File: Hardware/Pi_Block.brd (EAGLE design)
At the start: 30.5 x 94 mm, 54 parts, among them Q1 200mA/50V, U1 PCA9306, U2 EDISON_CONNECTOR_FULLMOUNTING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, U3 EDISON_CONNECTOR_FULLHEADER, U4 TPS62065, U5 MIC5219 3.3V, U6 TXB0108, U7 TXB0108

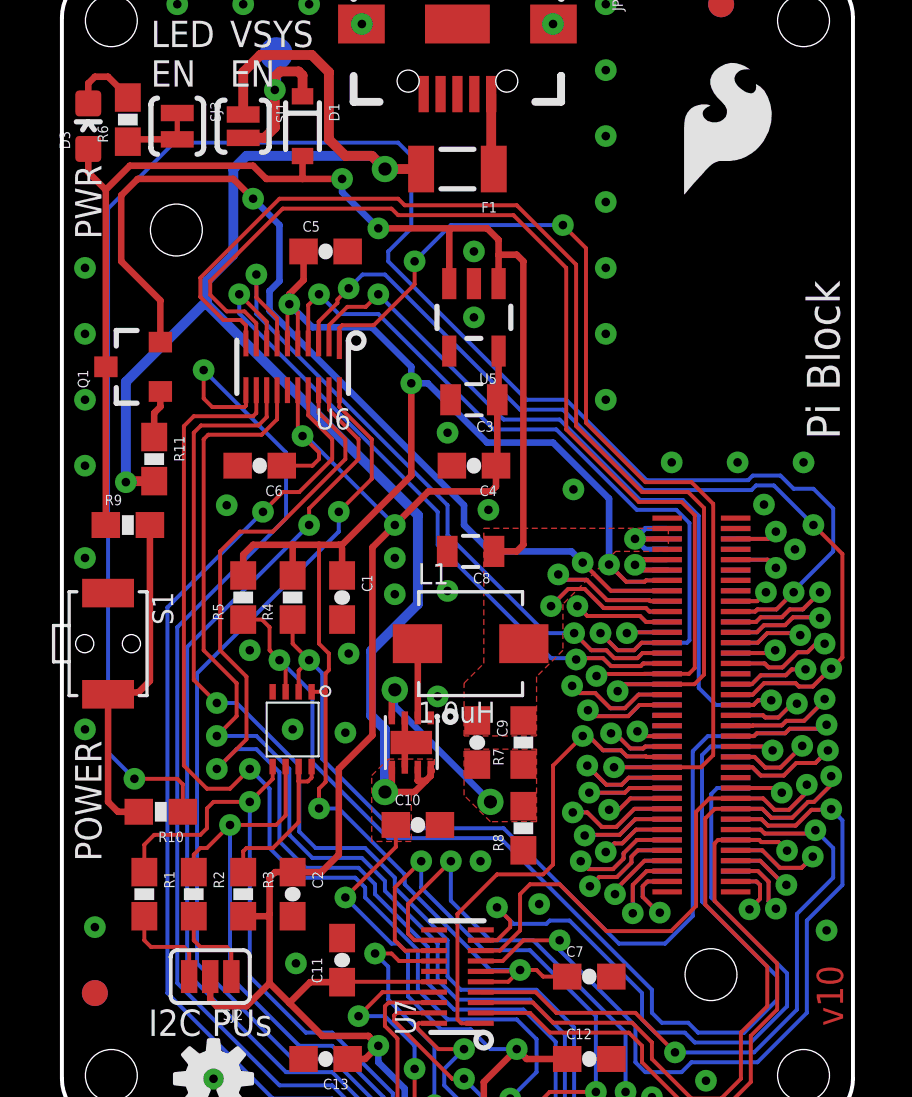
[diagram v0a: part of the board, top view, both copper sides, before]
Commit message: Fixed silk on PCA. Added dimensions.
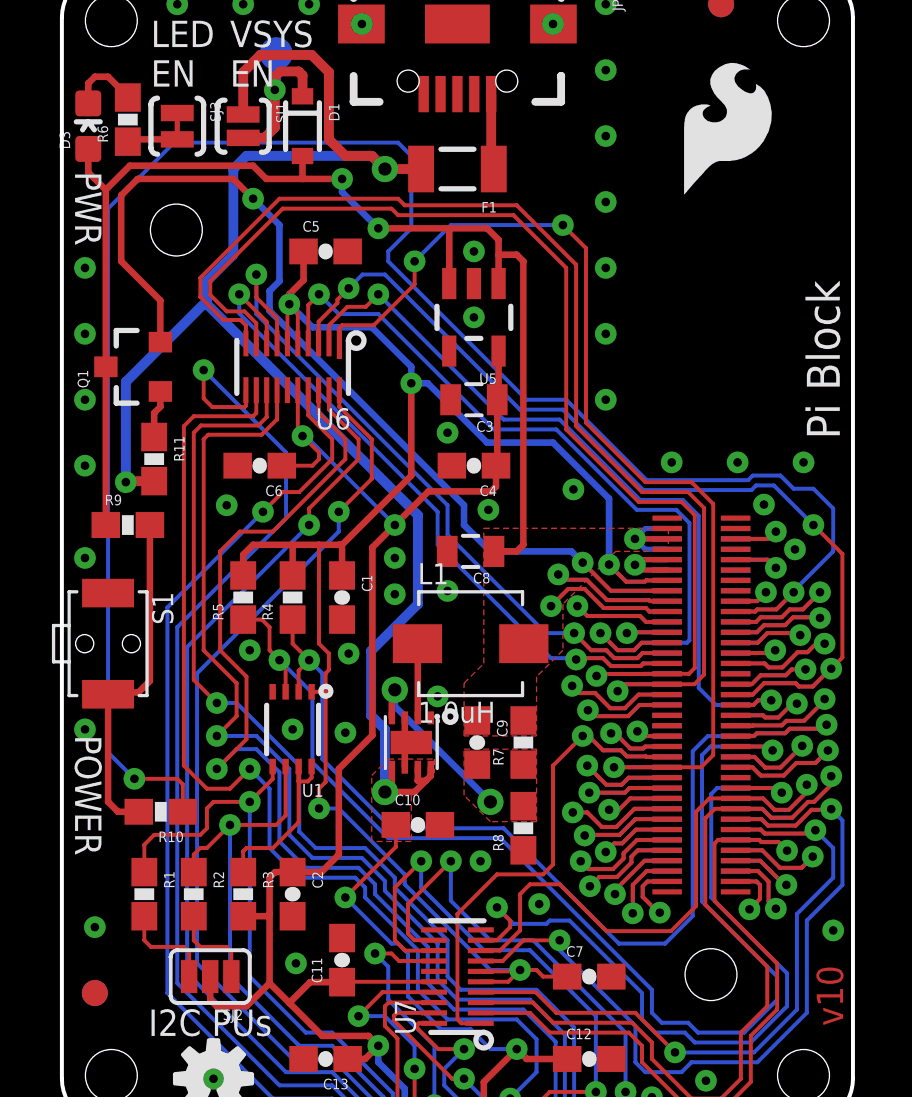
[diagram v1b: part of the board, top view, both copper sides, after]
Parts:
- moved FRAME1 7.62 mm to (-1.27, -66.0)
- moved FRAME2 7.62 mm to (-1.27, -66.0)
- moved FRAME3 7.62 mm to (-1.27, -66.0)
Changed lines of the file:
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@@
 <setting verticaltext="up"/>
 </settings>
-<grid distance="0.05" unitdist="inch" unit="inch" style="dots" multiple="1" display="yes" altdistance="0.005" altunitdist="inch" altunit="inch"/>
+<grid distance="0.1" unitdist="inch" unit="inch" style="dots" multiple="1" display="yes" altdistance="0.05" altunitdist="inch" altunit="inch"/>
 <layers>
 <layer number="1" name="Top" color="4" fill="1" visible="yes" active="yes"/>
@@
 <layer number="37" name="tTest" color="7" fill="1" visible="no" active="no"/>
 <layer number="38" name="bTest" color="7" fill="1" visible="no" active="no"/>
-<layer number="47" name="Measures" color="7" fill="1" visible="no" active="no"/>
+<layer number="47" name="Measures" color="7" fill="1" visible="no" active="yes"/>
 <layer number="48" name="Document" color="7" fill="1" visible="no" active="no"/>
 <layer number="49" name="Reference" color="7" fill="1" visible="no" active="no"/>
@@
 <wire x1="7.62" y1="0" x2="1.778" y2="0" width="0.1524" layer="20"/>
 <wire x1="0" y1="1.778" x2="0" y2="42.672" width="0.1524" layer="20"/>
-<text x="26.67" y="-58.42" size="1.6764" layer="51" ratio="15">Shawn Hymel</text>
+<text x="26.67" y="-66.04" size="1.6764" layer="51" ratio="15">Shawn Hymel</text>
 <hole x="28.575" y="1.905" drill="2"/>
 <hole x="1.905" y="1.905" drill="2"/>
@@
 <wire x1="1.778" y1="0" x2="0" y2="1.778" width="0.1524" layer="20" curve="-90"/>
 <wire x1="0" y1="42.672" x2="1.778" y2="44.45" width="0.1524" layer="20" curve="-90"/>
-<dimension x1="28.575" y1="1.905" x2="1.905" y2="1.905" x3="15.24" y3="46.99" textsize="1.27" textratio="15" layer="51" dtype="horizontal" unit="inch"/>
-<dimension x1="30.48" y1="1.728" x2="0" y2="2.54" x3="15.24" y3="49.53" textsize="1.27" textratio="15" layer="51" dtype="horizontal" unit="inch"/>
-<dimension x1="1.905" y1="42.545" x2="1.905" y2="1.905" x3="33.02" y3="22.225" textsize="1.27" textratio="15" layer="51" dtype="vertical" unit="inch"/>
-<dimension x1="1.778" y1="44.45" x2="5.08" y2="0" x3="35.56" y3="22.225" textsize="1.27" textratio="15" layer="51" dtype="vertical" unit="inch"/>
+<dimension x1="28.575" y1="1.905" x2="1.905" y2="1.905" x3="15.24" y3="46.99" textsize="1.27" textratio="15" layer="47" dtype="horizontal" unit="inch"/>
+<dimension x1="30.48" y1="1.728" x2="0" y2="2.54" x3="15.24" y3="49.53" textsize="1.27" textratio="15" layer="47" dtype="horizontal" unit="inch"/>
+<dimension x1="1.905" y1="42.545" x2="1.905" y2="1.905" x3="33.02" y3="22.225" textsize="1.27" textratio="15" layer="47" dtype="vertical" unit="inch"/>
+<dimension x1="1.778" y1="44.45" x2="5.08" y2="0" x3="35.56" y3="22.225" textsize="1.27" textratio="15" layer="47" dtype="vertical" unit="inch"/>
 <rectangle x1="22.098" y1="26.162" x2="30.48" y2="44.45" layer="42" rot="R180"/>
 <rectangle x1="22.098" y1="26.162" x2="30.48" y2="44.45" layer="41" rot="R180"/>
-<text x="29.21" y="6.35" size="1.016" layer="22" font="vector" ratio="15" rot="MR90" align="center">4xM2.0</text>
+<text x="29.21" y="6.35" size="1.016" layer="22" font="vector" ratio="15" rot="SMR270" align="center">4xM2.0</text>
 <text x="30.099" y="3.81" size="1.016" layer="1" font="vector" ratio="15" rot="R90">v10</text>
 <wire x1="10.16" y1="-49.53" x2="20.32" y2="-49.53" width="0.1524" layer="20"/>
-<text x="1.016" y="35.56" size="1.016" layer="21" font="vector" ratio="15" rot="R90" align="center">PWR</text>
-<text x="1.524" y="10.16" size="1.016" layer="21" font="vector" ratio="15" rot="R90">POWER</text>
+<text x="1.016" y="35.306" size="1.016" layer="21" font="vector" ratio="15" rot="SR270" align="center">PWR</text>
+<text x="1.016" y="12.7" size="1.016" layer="21" font="vector" ratio="15" rot="SR270" align="center">POWER</text>
 <text x="3.429" y="41.275" size="1.016" layer="21" font="vector" ratio="15" align="center-left">LED
 EN</text>
@@
 <text x="19.05" y="-7.62" size="1.016" layer="22" font="vector" ratio="15" rot="SMR270" align="top-center">5V</text>
 <text x="17.78" y="-10.16" size="1.016" layer="22" font="vector" ratio="15" rot="SMR270" align="top-center">5V</text>
-<text x="25.4" y="-5.08" size="1.778" layer="51" align="top-left">NOTES:
+<text x="-22.86" y="-2.54" size="1.778" layer="51" align="top-left">NOTES:
  - Board thickness = 0.063 in.</text>
 <hole x="15.24" y="-46.482" drill="2"/>
@@
 <wire x1="10.7696" y1="29.3624" x2="10.7696" y2="29.21" width="0.254" layer="41"/>
 <wire x1="10.7696" y1="29.21" x2="10.7696" y2="29.0322" width="0.254" layer="41"/>
+<wire x1="12.4968" y1="13.7922" x2="12.4968" y2="13.97" width="0.1524" layer="41"/>
+<wire x1="14.4018" y1="15.5956" x2="14.4018" y2="15.7734" width="0.1016" layer="41"/>
+<dimension x1="20.32" y1="-49.53" x2="27.94" y2="44.45" x3="41.148" y3="-2.54" textsize="1.778" textratio="15" layer="47" dtype="vertical" unit="inch"/>
+<dimension x1="10.16" y1="-49.53" x2="20.32" y2="-49.53" x3="15.24" y3="-55.626" textsize="1.778" textratio="15" layer="47" dtype="horizontal" unit="inch"/>
+<dimension x1="16.51" y1="-46.482" x2="27.432" y2="44.45" x3="45.466" y3="-1.016" textsize="1.778" textratio="15" layer="47" dtype="vertical" unit="inch"/>
+<dimension x1="15.24" y1="-47.752" x2="20.32" y2="-47.752" x3="17.78" y3="-52.324" textsize="1.778" textratio="15" layer="47" dtype="horizontal" unit="inch"/>
 </plain>
 <attributes>
@@
 </class>
 </classes>
-<designrules name="Pi_Block">
+<designrules name="Pi_Block *">
 <description language="en">&lt;b&gt;EAGLE Design Rules&lt;/b&gt;
 &lt;p&gt;
@@
 <param name="dpGapFactor" value="2.5"/>
 <param name="checkGrid" value="0"/>
-<param name="checkAngle" value="0"/>
+<param name="checkAngle" value="1"/>
 <param name="checkFont" value="1"/>
 <param name="checkRestrict" value="1"/>
@@
 <element name="U2" library="Edison" package="EDISON_DAUGHTER" value="EDISON_CONNECTOR_FULLMOUNTING_HOLES" x="27.94" y="3.81" rot="MR0"/>
 <element name="U3" library="Edison" package="DF40C-70DP-0.4(51)" value="EDISON_CONNECTOR_FULLHEADER" x="24.64" y="16.1798" rot="MR90"/>
-<element name="FRAME2" library="SparkFun-Aesthetics" package="CREATIVE_COMMONS" value="FRAME-LETTER" x="-1.27" y="-58.42"/>
+<element name="FRAME2" library="SparkFun-Aesthetics" package="CREATIVE_COMMONS" value="FRAME-LETTER" x="-1.27" y="-66.04"/>
 <element name="LOGO1" library="SparkFun-Aesthetics" package="OSHW-LOGO-S" value="OSHW-LOGOS" x="5.842" y="1.778"/>
 <element name="LOGO4" library="SparkFun-Aesthetics" package="SFE_LOGO_NAME_FLAME_.1" value="SFE_LOGO_NAME_FLAME.1_INCH" x="21.082" y="0.254" rot="MR0"/>
@@
 <attribute name="PROD_ID" value="IC-12292" x="15.24" y="5.715" size="1.778" layer="27" font="vector" ratio="15" rot="R90" display="off"/>
 </element>
-<element name="FRAME1" library="SparkFun-Aesthetics" package="CREATIVE_COMMONS" value="FRAME-LETTER" x="-1.27" y="-58.42"/>
-<element name="FRAME3" library="SparkFun-Aesthetics" package="CREATIVE_COMMONS" value="FRAME-LETTER" x="-1.27" y="-58.42"/>
+<element name="FRAME1" library="SparkFun-Aesthetics" package="CREATIVE_COMMONS" value="FRAME-LETTER" x="-1.27" y="-66.04"/>
+<element name="FRAME3" library="SparkFun-Aesthetics" package="CREATIVE_COMMONS" value="FRAME-LETTER" x="-1.27" y="-66.04"/>
 <element name="TP1" library="SparkFun-Passives" package="PAD.03X.05" value="TEST-POINT3X5" x="8.255" y="41.275" rot="MR0"/>
 </elements>
@@
 <via x="13.97" y="-3.556" extent="1-16" drill="0.3302"/>
 <via x="15.748" y="-5.08" extent="1-16" drill="0.3302"/>
-<via x="29.464" y="7.493" extent="1-16" drill="0.3302"/>
+<via x="29.718" y="7.493" extent="1-16" drill="0.3302"/>
 <via x="0.889" y="33.02" extent="1-16" drill="0.3302"/>
 <via x="0.889" y="30.48" extent="1-16" drill="0.3302"/>
